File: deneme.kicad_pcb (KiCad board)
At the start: 2 copper layers, 79 x 66.8 mm, 70 parts, among them J1 USB_C_Receptacle_USB2.0_16P, J2 Conn_01x04_Pin, J3 LORA_USART2_SOCKETS, J4 RJ45, SW1 SW_SPDT, U1 STM32F103C8T6, U2 AMS1117-3.3, U3 MAX485E, U4 ESDS302DBVR, U5 USBLC6-2SC6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

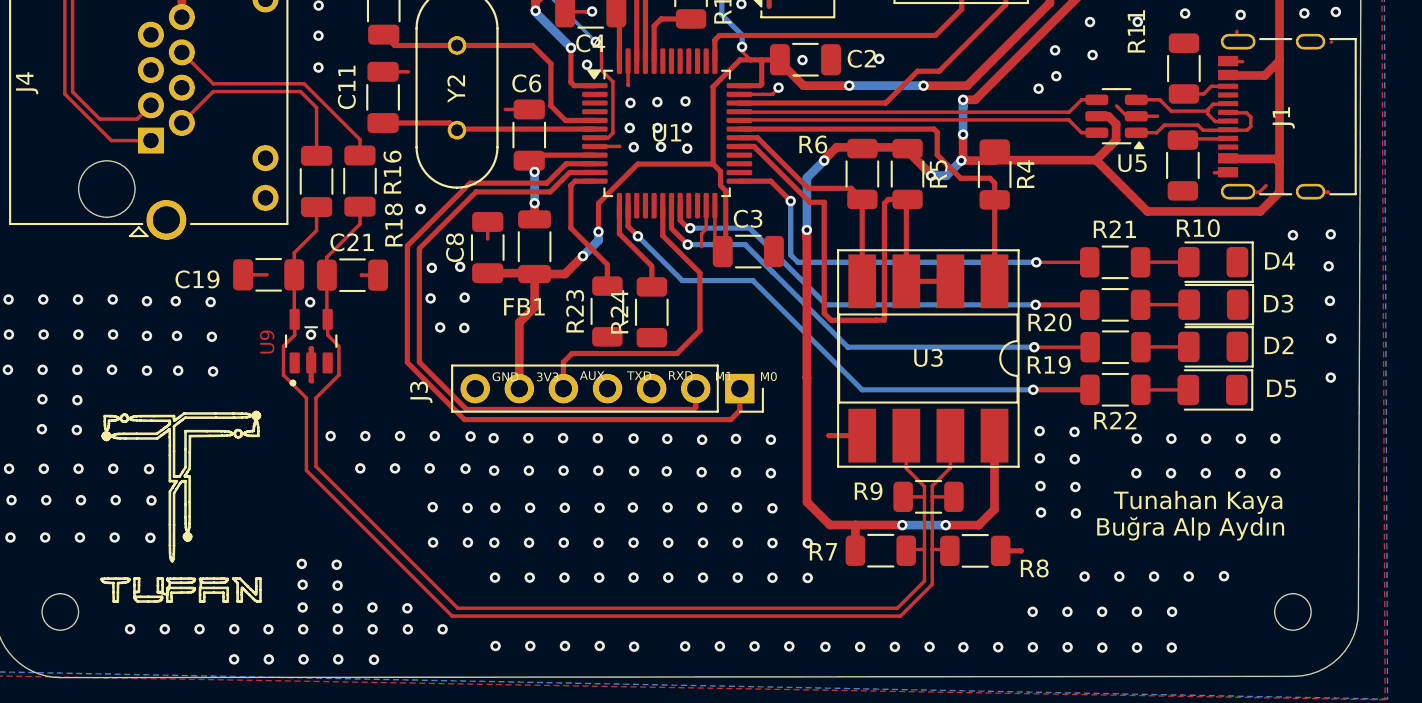
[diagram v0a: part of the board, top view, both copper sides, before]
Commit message: Added Ibrahım Gul's name to the board
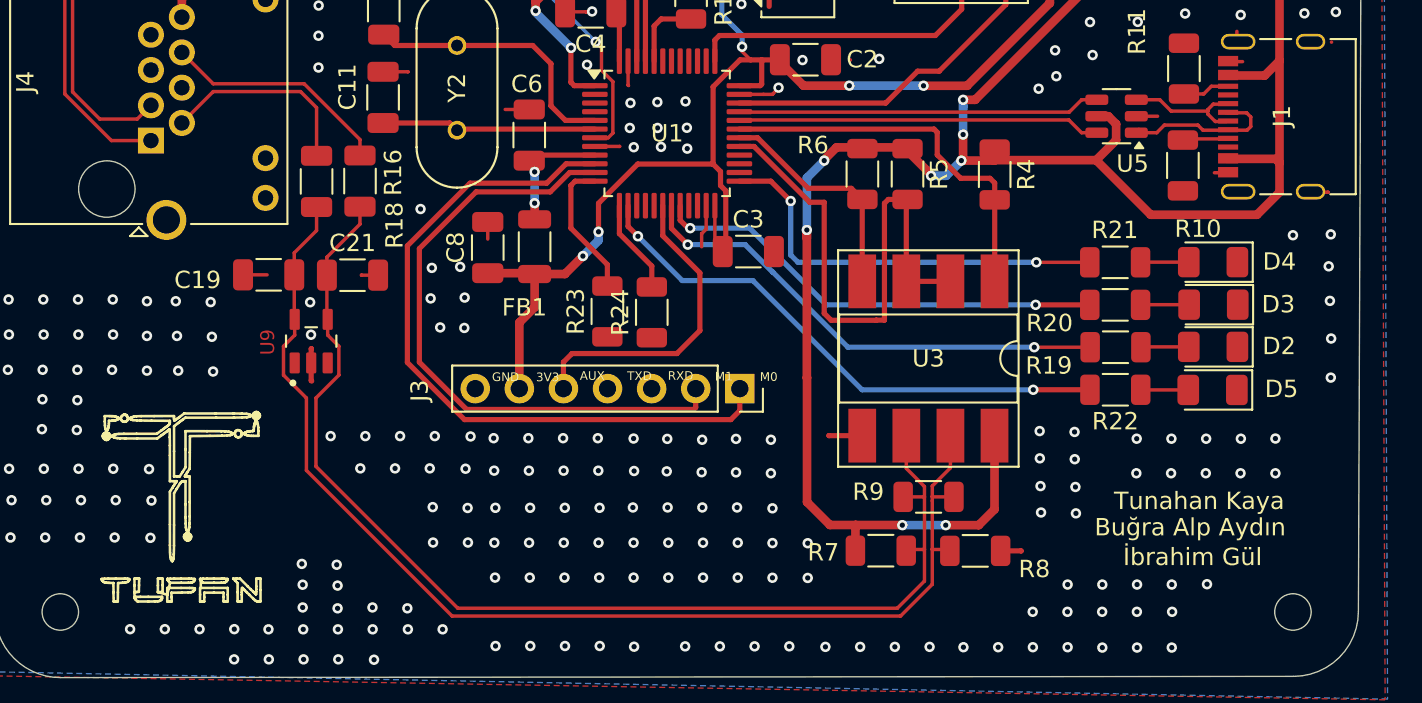
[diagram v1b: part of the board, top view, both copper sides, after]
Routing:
- net GND: track 50.0 -> 47.3 mm
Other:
- board text added: "İbrahim Gül"
